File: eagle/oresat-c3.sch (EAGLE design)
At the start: 161 parts, among them J1 J-SAMTEC-TFM-110-X1-XXX-D-RA, J10 U.FL, J11 U.FL, J13 U.FL, J14 U.FL, J15 HARWIN-2X8X1.27, J19 HARWIN-2X8X1.27, J2 U.FL, J3 U.FL, J4 U.FL, J6 J-SAMTEC-TFM-120-X1-XXX-D-RA, J7 FTSH-105-XX-X-DV-K, J8 U.FL, J9 U.FL, Q1 MOSFET-PCH-SOT23-6, U1 MAX892LEUA+T21-0036K-L, U11 U-ONSEMI-AX5043, U12 LP2985XX-N, U13 U-ONSEMI-AX5043, U14 LP2985XX-N, U2 TCAN330, U3 TCAN330, U4 TPS259621 - eFuse, U5 TPS62111RSA, U6 MAX6374KA-T21-0078H-L, U7 STM32F446RE, U9 SFEM016GB1EM1TO-A-HG-111-STD, X1 16MHZ-2.5x2mm, X3 TAITIEN-TY, X4 TAITIEN-TY

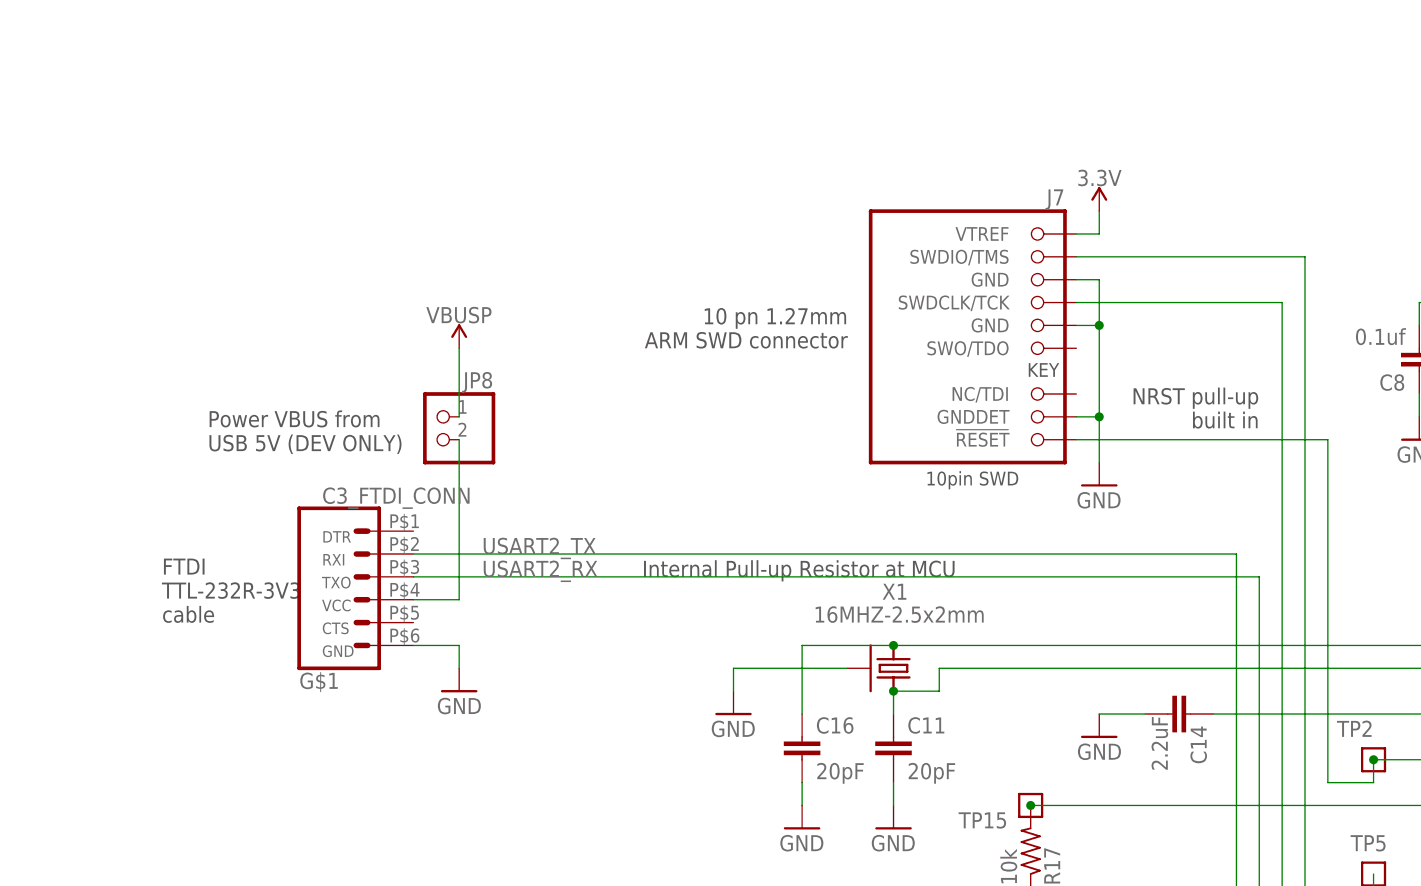
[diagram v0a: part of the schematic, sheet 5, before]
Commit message: Moving and removing
Moved everything left (incomplete)
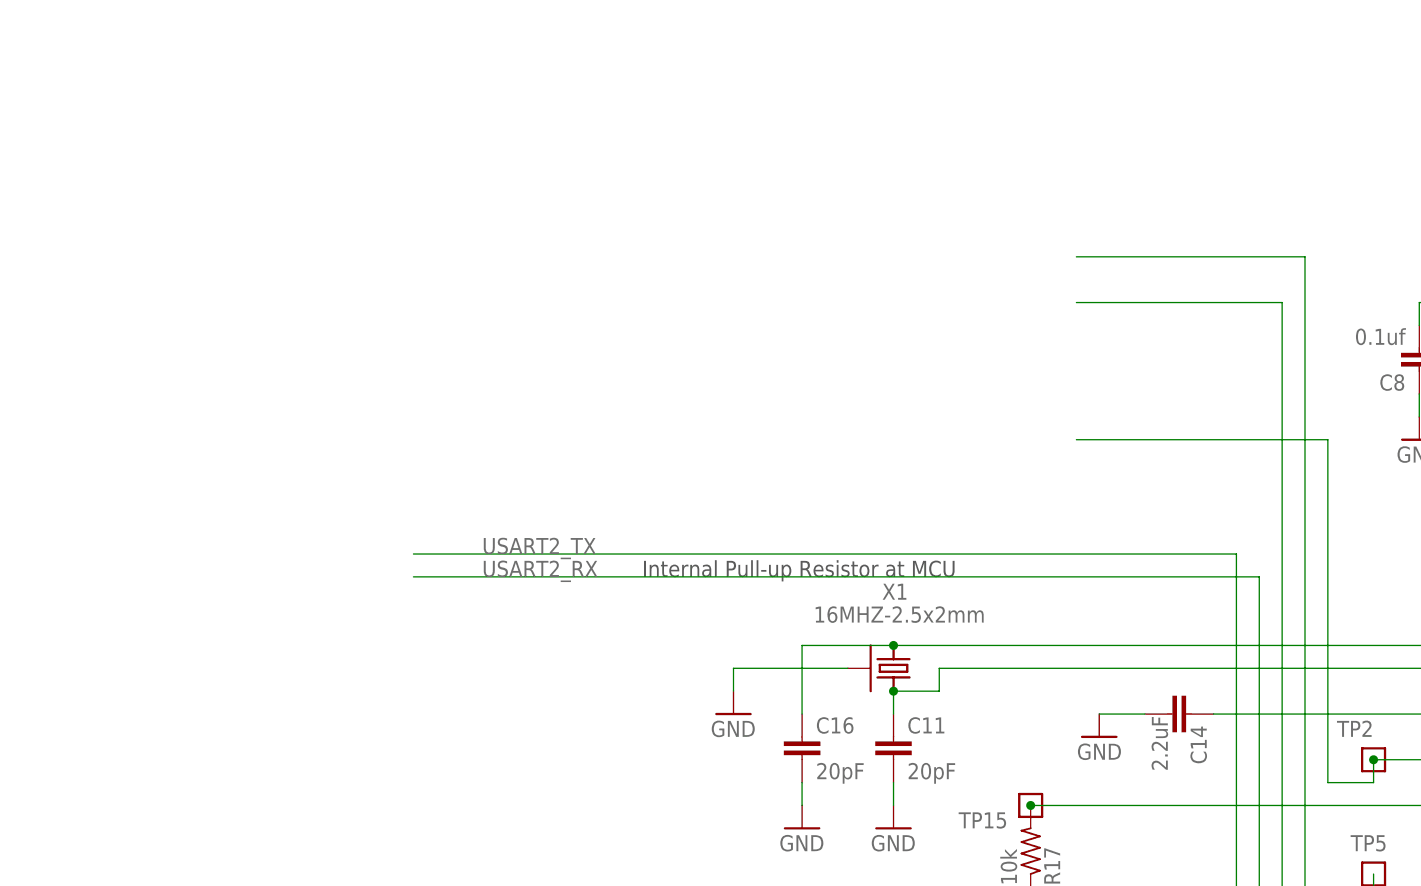
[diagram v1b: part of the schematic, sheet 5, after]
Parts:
- removed J7: FTSH-105-XX-X-DV-K, J-Samtec-FTSH-105-XXX-DV-K-ARM-SWD:FTSH-105-XX-X-DV-K
- removed JP8: (no value), pinhead:PINHD-1X2
- removed JP9: (no value), pinhead:PINHD-1X10
- removed U$2: C3_FTDI_CONN, TrueC3_FTDIlbr:C3_FTDI_CONN
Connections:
- removed net N$406: JP8.2, U$2.VCC
- net 3.3V: no longer J7.VTREF
- net AUX-1: no longer JP9.1
- net AUX-2: no longer JP9.2
- net AUX-3: no longer JP9.3
- net AUX-4: no longer JP9.4
- net AUX-5: no longer JP9.5
- net AUX-6: no longer JP9.6
- net AUX-7: no longer JP9.7
- net AUX-8: no longer JP9.8
- net AUX-9: no longer JP9.9
- net AUX_!SHUTDOWN: no longer JP9.10
- net GND: no longer J7.GND, J7.GND@2, J7.GNDDET, U$2.GND
- net NRST: no longer J7.!RESET
- net SWCLK: no longer J7.SWDCLK/TCK
- net SWDIO: no longer J7.SWDIO/TMS
- net USART2_RX: no longer U$2.TXO
- net USART2_TX: no longer U$2.RXI
- net VBUSP: no longer JP8.1
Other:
- note removed: "10 pn 1.27mm ARM SWD connector"
- note removed: "FTDI TTL-232R-3V3 cable"
- note removed: "NRST pull-up built in"
- note removed: "Power VBUS from USB 5V (DEV ONLY)"

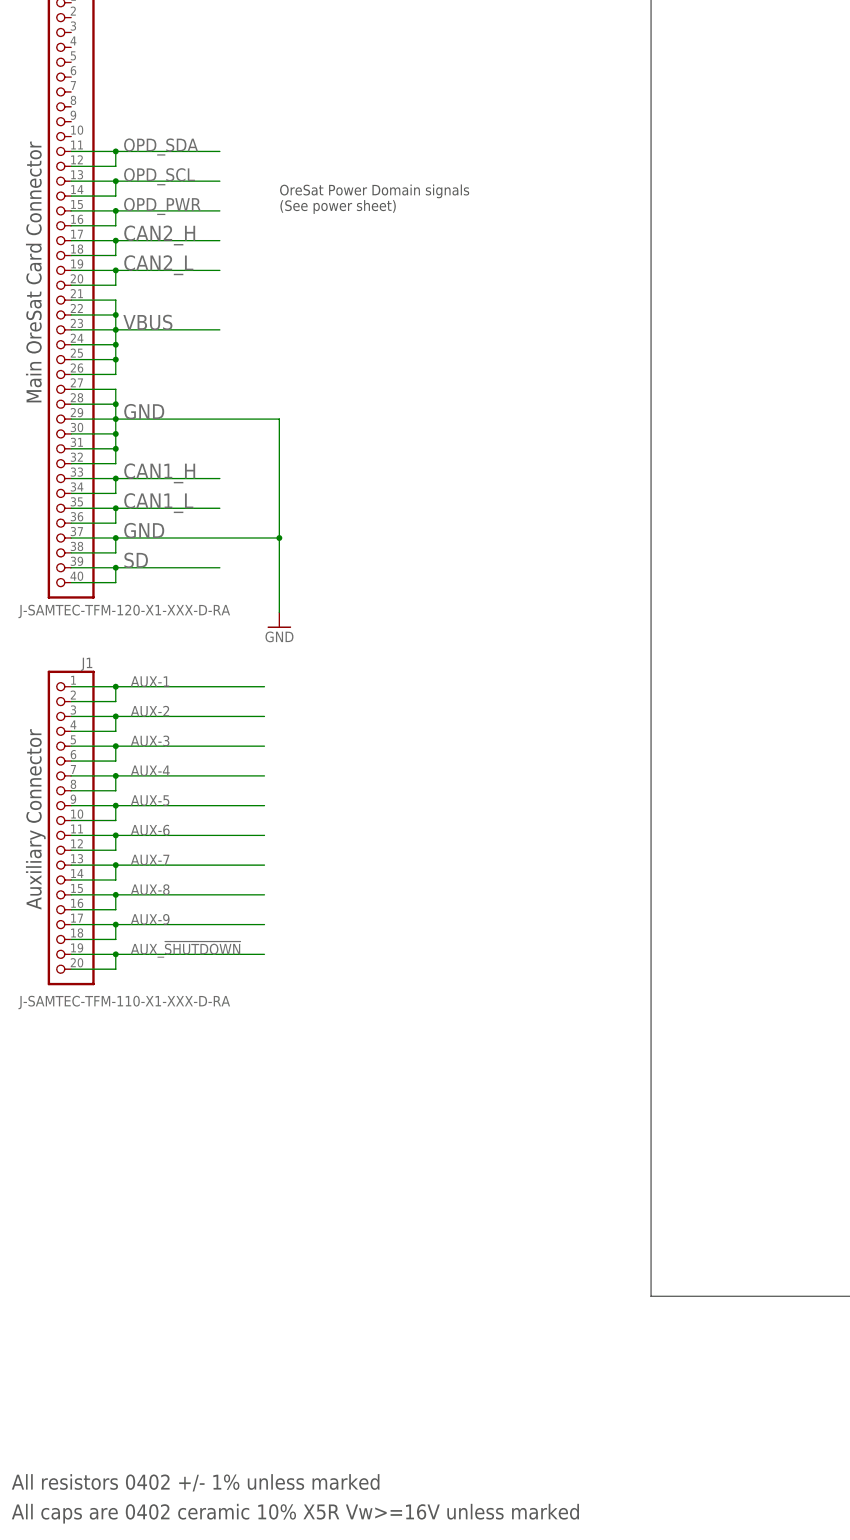
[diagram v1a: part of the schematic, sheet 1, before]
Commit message: Added edge connector, TVS
Moved to the left mostly connected
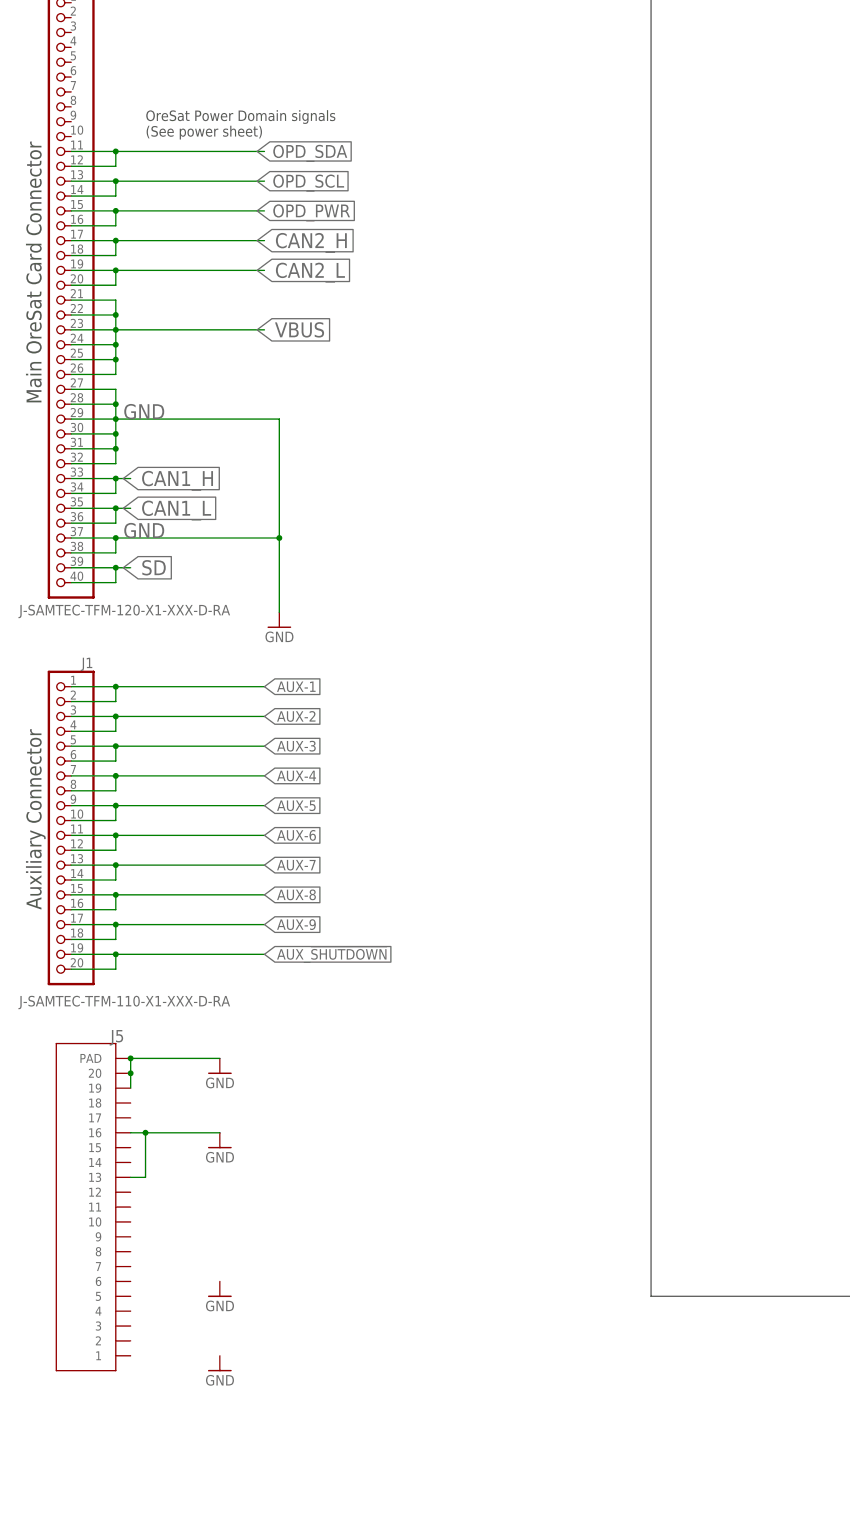
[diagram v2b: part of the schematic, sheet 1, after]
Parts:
- added D6: SZ1SMB5.0AT3G, D-LittelFuse-Uni-Directional-TVS:SZ1SMB5.0AT3G
- added J5: 2-1734592-0, J-TEConnectivity-X-1734592-X:2-1734592-0
- added R18: 0, C3_SamacSys_Parts:R0603-0-OHMS
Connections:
- new net OPD_SDA_P: R11.2, R18.1, U7.PB9
- net GND: now also D6.A, J5.13, J5.16, J5.19, J5.20, J5.PAD
- net OPD_SDA: now also D6.K, R18.2; no longer R11.2, U7.PB9
- net SDIO_CK: now also R14.77; no longer R14.22
- net SDIO_CMD: now also R14.44; no longer R14.99
- net SDIO_D0: now also R14.88; no longer R15.11
- net SDIO_D1: now also R14.11; no longer R15.99
- net SDIO_D2: now also R14.99; no longer R15.22
- net SDIO_D3: now also R14.22; no longer R14.77
- net SDIO_D4: now also R14.33; no longer R14.66
- net SDIO_D5: now also R14.66; no longer R14.88
- net SDIO_D6: now also R15.11; no longer R14.44
- net SDIO_D7: now also R15.99; no longer R15.33
- net SDIO_RST: now also R15.22; no longer R14.33
